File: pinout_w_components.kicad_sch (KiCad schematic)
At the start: 41 parts, among them J1 10155435-00011LF, U10 ESDS304DBVR, U11 ESD351DPYR, U12 TJA1051TK-3, U9 ESDS304DBVR

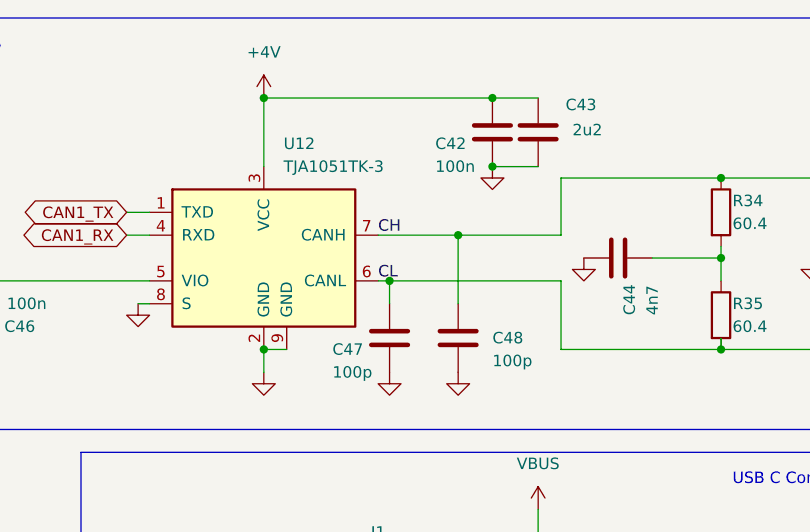
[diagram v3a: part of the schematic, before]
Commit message: remove blind vias and use 0201 resistors
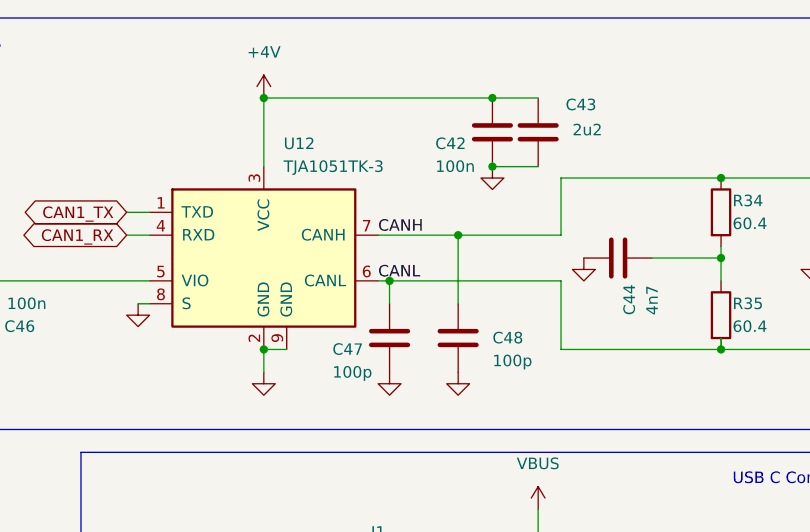
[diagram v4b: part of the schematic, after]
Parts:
- C42, C46: footprint Capacitor_SMD:C_0402_1005Metric -> Project:C_0201_0603Metric; Manufactorer YAGEO -> Murata; Part Number CC0402KRX5R8BB104 -> GRM033R61E104KE14J
- C43, C45: footprint Capacitor_SMD:C_0603_1608Metric -> Capacitor_SMD:C_0402_1005Metric; Manufactorer Murata -> YAGEO; Part Number GRM188R61E225KA12D -> CC0402KPX5R8BB225
- C44: Part Number GRM155R61H472KA01D -> GRM155R61H472KA01D; Tolerance 5% -> 10%
- D10: Color Yellow -> Orange
- R27: footprint Resistor_SMD:R_0402_1005Metric -> Project:R_0201_0603Metric; Part Number RC0402FR-07680RP -> RC0201FR-07680RL
- R28: footprint Resistor_SMD:R_0402_1005Metric -> Project:R_0201_0603Metric; Part Number RT0402BRD0722K1L -> RC0201FR-0722K1L; Tolerance 0.1% -> 1%
- R29: footprint Resistor_SMD:R_0402_1005Metric -> Project:R_0201_0603Metric; Part Number RT0402BRD073K3L -> RC0201FR-073K3L; Tolerance 0.1% -> 1%
- R30, R32: footprint Resistor_SMD:R_0402_1005Metric -> Project:R_0201_0603Metric; Part Number RC0402FR-070RL -> RC0201FR-070RL; Tolerance 0.1% -> (none)
- R31: footprint Resistor_SMD:R_0402_1005Metric -> Project:R_0201_0603Metric; Part Number RC0402JR-0710ML -> RC0201FR-071ML; Tolerance 0.1% -> 1%
- R33: footprint Resistor_SMD:R_0402_1005Metric -> Project:R_0201_0603Metric; Part Number RC0402JR-0710ML -> RC0201FR-071ML; Tolerance 5% -> 1%
- R34, R35: footprint Resistor_SMD:R_0402_1005Metric -> Project:R_0201_0603Metric; Part Number RC0402FR-0760R4L -> RC0201FR-0760R4L
- R36, R37: footprint Resistor_SMD:R_0402_1005Metric -> Project:R_0201_0603Metric; Part Number RC0402FR-075K1L -> RC0201FR-075K1L
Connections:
- net CH renamed CANH
- net CL renamed CANL
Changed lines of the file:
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@@
 		)
 	)
-	(label "CL"
+	(label "CANL"
 		(at 208.28 44.45 0)
 		(fields_autoplaced yes)
@@
 		)
 	)
-	(label "CH"
+	(label "CANH"
 		(at 208.28 39.37 0)
 		(fields_autoplaced yes)
@@
 			)
 		)
-		(property "Footprint" "Resistor_SMD:R_0402_1005Metric"
+		(property "Footprint" "Project:R_0201_0603Metric"
 			(at 117.602 153.67 90)
 			(effects
@@
 			)
 		)
-		(property "Tolerance" "0.1%"
+		(property "Tolerance" "1%"
 			(at 119.38 153.67 0)
 			(effects
@@
 			)
 		)
-		(property "Part Number" "RC0402JR-0710ML"
+		(property "Part Number" "RC0201FR-071ML"
 			(at 119.38 153.67 0)
 			(effects
@@
 			)
 		)
-		(property "Footprint" "Capacitor_SMD:C_0402_1005Metric"
+		(property "Footprint" "Project:C_0201_0603Metric"
 			(at 162.8648 44.45 0)
 			(effects
@@
 			)
 		)
-		(property "Manufactorer" "YAGEO"
+		(property "Manufactorer" "Murata"
 			(at 163.83 48.26 0)
 			(effects
@@
 			)
 		)
-		(property "Part Number" "CC0402KRX5R8BB104"
+		(property "Part Number" "GRM033R61E104KE14J"
 			(at 163.83 48.26 0)
 			(effects
@@
 			)
 		)
-		(property "Footprint" "Capacitor_SMD:C_0402_1005Metric"
+		(property "Footprint" "Project:C_0201_0603Metric"
 			(at 221.9452 31.75 0)
 			(effects
@@
 			)
 		)
-		(property "Manufactorer" "YAGEO"
+		(property "Manufactorer" "Murata"
 			(at 220.98 27.94 0)
 			(effects
@@
 			)
 		)
-		(property "Part Number" "CC0402KRX5R8BB104"
+		(property "Part Number" "GRM033R61E104KE14J"
 			(at 220.98 27.94 0)
 			(effects
@@
 			)
 		)
-		(property "Footprint" "Resistor_SMD:R_0402_1005Metric"
+		(property "Footprint" "Project:R_0201_0603Metric"
 			(at 244.602 48.26 90)
 			(effects
@@
 			)
 		)
-		(property "Part Number" "RC0402FR-0760R4L"
+		(property "Part Number" "RC0201FR-0760R4L"
 			(at 246.38 48.26 0)
 			(effects
@@
 			)
 		)
-		(property "Footprint" "Resistor_SMD:R_0402_1005Metric"
+		(property "Footprint" "Project:R_0201_0603Metric"
 			(at 117.602 143.51 90)
 			(effects
@@
 			)
 		)
-		(property "Tolerance" "0.1%"
+		(property "Tolerance" ""
 			(at 119.38 143.51 0)
 			(effects
@@
 			)
 		)
-		(property "Part Number" "RC0402FR-070RL"
+		(property "Part Number" "RC0201FR-070RL"
 			(at 119.38 143.51 0)
 			(effects
@@
 			)
 		)
-		(property "Footprint" "Resistor_SMD:R_0402_1005Metric"
+		(property "Footprint" "Project:R_0201_0603Metric"
 			(at 185.42 83.312 90)
 			(effects
@@
 			)
 		)
-		(property "Part Number" "RC0402FR-075K1L"
+		(property "Part Number" "RC0201FR-075K1L"
 			(at 185.42 85.09 0)
 			(effects
@@
 			)
 		)
-		(property "Footprint" "Resistor_SMD:R_0402_1005Metric"
+		(property "Footprint" "Project:R_0201_0603Metric"
 			(at 231.14 93.472 90)
 			(effects
@@
 			)
 		)
-		(property "Part Number" "RC0402FR-075K1L"
+		(property "Part Number" "RC0201FR-075K1L"
 			(at 231.14 95.25 0)
 			(effects
@@
 			)
 		)
-		(property "Footprint" "Resistor_SMD:R_0402_1005Metric"
+		(property "Footprint" "Project:R_0201_0603Metric"
 			(at 117.602 114.3 90)
 			(effects
@@
 			)
 		)
-		(property "Tolerance" "0.1%"
+		(property "Tolerance" "1%"
 			(at 119.38 114.3 0)
 			(effects
@@
 			)
 		)
-		(property "Part Number" "RT0402BRD0722K1L"
+		(property "Part Number" "RC0201FR-0722K1L"
 			(at 119.38 114.3 0)
 			(effects
@@
 			)
 		)
-		(property "Footprint" "Resistor_SMD:R_0402_1005Metric"
+		(property "Footprint" "Project:R_0201_0603Metric"
 			(at 244.602 36.83 90)
 			(effects
@@
 			)
 		)
-		(property "Part Number" "RC0402FR-0760R4L"
+		(property "Part Number" "RC0201FR-0760R4L"
 			(at 246.38 36.83 0)
 			(effects
@@
 			)
 		)
-		(property "Footprint" "Resistor_SMD:R_0402_1005Metric"
+		(property "Footprint" "Project:R_0201_0603Metric"
 			(at 117.602 182.88 90)
 			(effects
@@
 			)
 		)
-		(property "Tolerance" "5%"
+		(property "Tolerance" "1%"
 			(at 119.38 182.88 0)
 			(effects
@@
 			)
 		)
-		(property "Part Number" "RC0402JR-0710ML"
+		(property "Part Number" "RC0201FR-071ML"
 			(at 119.38 182.88 0)
 			(effects
@@
 			)
 		)
-		(property "Footprint" "Capacitor_SMD:C_0603_1608Metric"
+		(property "Footprint" "Capacitor_SMD:C_0402_1005Metric"
 			(at 153.3652 52.07 0)
 			(effects
@@
 			)
 		)
-		(property "Manufactorer" "Murata"
+		(property "Manufactorer" "YAGEO"
 			(at 152.4 48.26 0)
 			(effects
@@
 			)
 		)
-		(property "Part Number" "GRM188R61E225KA12D"
+		(property "Part Number" "CC0402KPX5R8BB225"
 			(at 152.4 48.26 0)
 			(effects
@@
 			)
 		)
-		(property "Part Number" "GRM155R61H472KA01D "
+		(property "Part Number" "GRM155R61H472KA01D"
 			(at 234.95 41.91 0)
 			(effects
@@
 			)
 		)
-		(property "Tolerance" "5%"
+		(property "Tolerance" "10%"
 			(at 234.95 41.91 0)
 			(effects
@@
 			)
 		)
-		(property "Footprint" "Resistor_SMD:R_0402_1005Metric"
+		(property "Footprint" "Project:R_0201_0603Metric"
 			(at 132.588 86.36 90)
 			(effects
@@
 			)
 		)
-		(property "Part Number" "RC0402FR-07680RP"
+		(property "Part Number" "RC0201FR-07680RL"
 			(at 130.81 86.36 0)
 			(effects
@@
 			)
 		)
-		(property "Footprint" "Resistor_SMD:R_0402_1005Metric"
+		(property "Footprint" "Project:R_0201_0603Metric"
 			(at 117.602 172.72 90)
 			(effects
@@
 			)
 		)
-		(property "Part Number" "RC0402FR-070RL"
+		(property "Part Number" "RC0201FR-070RL"
 			(at 119.38 172.72 0)
 			(effects
@@
 			)
 		)
-		(property "Tolerance" "0.1%"
+		(property "Tolerance" ""
 			(at 119.38 172.72 0)
 			(effects
@@
 			)
 		)
-		(property "Footprint" "Resistor_SMD:R_0402_1005Metric"
+		(property "Footprint" "Project:R_0201_0603Metric"
 			(at 117.602 124.46 90)
 			(effects
@@
 			)
 		)
-		(property "Tolerance" "0.1%"
+		(property "Tolerance" "1%"
 			(at 119.38 124.46 0)
 			(effects
@@
 			)
 		)
-		(property "Part Number" "RT0402BRD073K3L"
+		(property "Part Number" "RC0201FR-073K3L"
 			(at 119.38 124.46 0)
 			(effects
@@
 			)
 		)
-		(property "Footprint" "Capacitor_SMD:C_0603_1608Metric"
+		(property "Footprint" "Capacitor_SMD:C_0402_1005Metric"
 			(at 227.0252 31.75 0)
 			(effects
@@
 			)
 		)
-		(property "Manufactorer" "Murata"
+		(property "Manufactorer" "YAGEO"
 			(at 226.06 27.94 0)
 			(effects
@@
 			)
 		)
-		(property "Part Number" "GRM188R61E225KA12D"
+		(property "Part Number" "CC0402KPX5R8BB225"
 			(at 226.06 27.94 0)
 			(effects
@@
 			)
 		)
-		(property "Color" "Yellow"
+		(property "Color" "Orange"
 			(at 130.81 78.74 90)
 			(effects

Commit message: double check BOM
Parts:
- C43, C45: Manufactorer YAGEO -> Murata; Part Number CC0402KPX5R8BB225 -> GRT155R61E225KE13D
- C47, C48: Manufactorer YAGEO -> Murata; Part Number CC0402JRNPO9BN101 -> GRM1555C1H101JA01D
- D10: Voltage (none) -> 2
- R31, R33: Part Number RC0201FR-071ML -> RC0201FR-0710ML
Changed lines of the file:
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@@
 			)
 		)
-		(property "Part Number" "RC0201FR-071ML"
+		(property "Part Number" "RC0201FR-0710ML"
 			(at 119.38 153.67 0)
 			(effects
@@
 			)
 		)
-		(property "Manufactorer" "YAGEO"
+		(property "Manufactorer" "Murata"
 			(at 209.55 50.8 0)
 			(effects
@@
 			)
 		)
-		(property "Part Number" "CC0402JRNPO9BN101"
+		(property "Part Number" "GRM1555C1H101JA01D"
 			(at 209.55 50.8 0)
 			(effects
@@
 			)
 		)
-		(property "Part Number" "RC0201FR-071ML"
+		(property "Part Number" "RC0201FR-0710ML"
 			(at 119.38 182.88 0)
 			(effects
@@
 			)
 		)
-		(property "Manufactorer" "YAGEO"
+		(property "Manufactorer" "Murata"
 			(at 152.4 48.26 0)
 			(effects
@@
 			)
 		)
-		(property "Part Number" "CC0402KPX5R8BB225"
+		(property "Part Number" "GRT155R61E225KE13D"
 			(at 152.4 48.26 0)
 			(effects
@@
 			)
 		)
-		(property "Manufactorer" "YAGEO"
+		(property "Manufactorer" "Murata"
 			(at 217.17 50.8 0)
 			(effects
@@
 			)
 		)
-		(property "Part Number" "CC0402JRNPO9BN101"
+		(property "Part Number" "GRM1555C1H101JA01D"
 			(at 217.17 50.8 0)
 			(effects
@@
 			)
 		)
-		(property "Manufactorer" "YAGEO"
+		(property "Manufactorer" "Murata"
 			(at 226.06 27.94 0)
 			(effects
@@
 			)
 		)
-		(property "Part Number" "CC0402KPX5R8BB225"
+		(property "Part Number" "GRT155R61E225KE13D"
 			(at 226.06 27.94 0)
 			(effects
@@
 			(at 130.81 78.74 0)
 			(effects
+				(font
+					(size 1.27 1.27)
+				)
+				(hide yes)
+			)
+		)
+		(property "Voltage" "2"
+			(at 130.81 78.74 0)
+			(effects
